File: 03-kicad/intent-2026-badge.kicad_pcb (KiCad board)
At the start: 2 copper layers, 56 x 118 mm, 89 parts, among them J1 TYPE-C-16PIN, J2 HACK HEADER, J3 BATT 3xAAA, J4 PJ-320D, J5 IR, J6 AUDIO, J7 SPK, P1 IR MODULE, P2 AUDIO MODULE, P3 SPK MODULE, Q1 HL3401, Q2 S8050, SW1 BOOTSEL, SW2 A, SW3 B, SW4 C, SW5 MSK12C02, U1 RP2040, U2 W25Q16JVSNIQ, U3 ME6206A33M3G, U4 USBLC6-2SC6, U5 IRM-H638T/TR2, Y1 12MHz

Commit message: Vending-machine theme: themed silkscreen, modules as vended items with shaped outlines
- silk.py: shelf items A1-A4 with price tags over a dispensing coil, keypad bezel + SELECT,
  CREDIT meter with coin values, ITEM PICKUP door around slots B1/B2/B3, coin slot,
  back service-panel texts (SERVICE COMPARTMENT, model plate, NO REFUNDS)
- modules: B1 EYE CANDY candy bar (crimped edges, 1.2 mm chamfers), B2 AUDIO POP soda can
  (R 2.5 corners, bubbles), B3 BEEP CHIPS chips bag (crimped edges, 2 mm chamfers)
- placement.MODULE_CORNERS + pcb_build.module_perimeter/add_module_edges draw the corners
- board, gerbers, renders, DRC/ERC reports regenerated (DRC 0 violations); docs updated

Co-Authored-By: Claude Fable 5.1 <noreply@anthropic.com>
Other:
- outline, holes or cut-outs redrawn
- board text added: "$1"
- board text added: "10¢"
- board text added: "25¢"
- board text added: "38kHz"
- board text added: "50¢"
- board text added: "5¢"
- board text added: "A1 25¢"
- board text added: "A2 50¢"
- board text added: "A3 75¢"
- board text added: "A4 $1"
- board text added: "AUDIO POP · 3.5mm"
- board text added: "AUTHORIZED PERSONNEL ONLY"
- board text added: "B1"
- board text added: "B1 IR"
- board text added: "B1 · IR MODULE"
- board text added: "B2"
- board text added: "B2 AUDIO"
- board text added: "B2 · AUDIO MODULE"
- board text added: "B3"
- board text added: "B3 SPK"
- board text added: "B3 · SPK MODULE"
- board text added: "BEEP CHIPS"
- board text added: "EYE CANDY"
- board text added: "ITEM PICKUP"
- board text added: "MODEL VM-2026 · 3V3 · 2 LAYERS"
- board text added: "NO REFUNDS · DO NOT TILT OR ROCK"
- board text added: "NO USER-SERVICEABLE PARTS INSIDE (JK, SEE J2)"
- board text added: "SELECT"
- board text added: "SERVICE COMPARTMENT"
- board text added: "← PRIZE"
- board text removed: "* PRIZE *"
- board text removed: "AUDIO"
- board text removed: "AUDIO MODULE"
- board text removed: "IR EYE"
- board text removed: "IR MODULE"
- board text removed: "SPK"
- board text removed: "SPK MODULE"

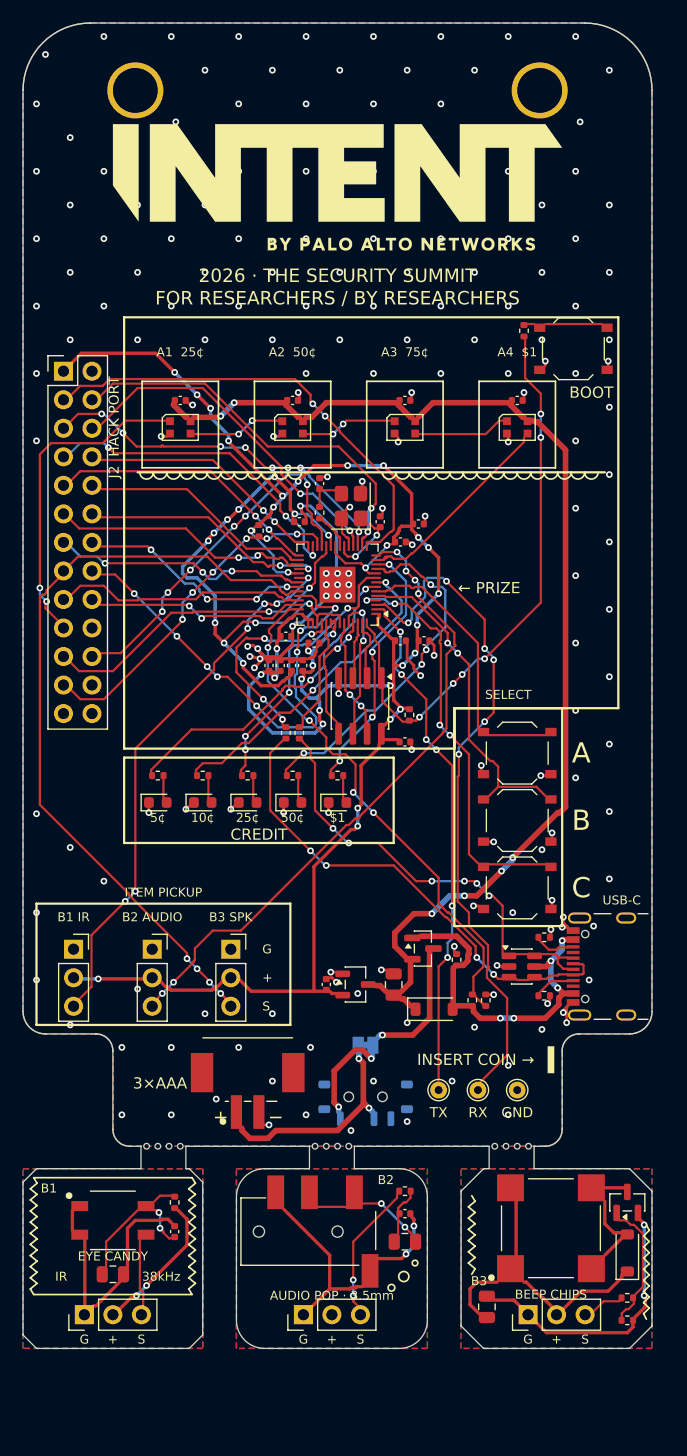
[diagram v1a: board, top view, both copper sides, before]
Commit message: Vending-machine outline: header sign box with lanyard holes, modules as 13x22 mm soda cans
- pcb_build OUTLINE: R6 top replaced by a header sign box x 7-49 x y 0-9 (R2.5 corners, R1 fillets,
  R2 cabinet corners); H1/H2 moved to (12,5.5)/(44,5.5); INTENT-O-MATIC marquee; logo 1 mm lower
- placement: MODULES = cans 13x22 R2.2 at x 5.5/21.5/37.5, tabs 12/28/44, blank 56x124;
  module parts re-placed (header at the can bottom, passives in a row)
- silk: can rims, label band with wave, B1 IR COLA / B2 AUDIO POP / B3 BEEP FIZZ
- router: NY 1270, NET_ONLY mode + router/prune_routes.py for partial re-routes; only module
  nets re-routed (97 tracks, 14 vias), main-board copper unchanged except 8 pruned edge GND vias
- board, gerbers, CPL, renders, reports regenerated: DRC 0 violations, 0 unconnected; docs updated

Co-Authored-By: Claude Fable 5.1 <noreply@anthropic.com>
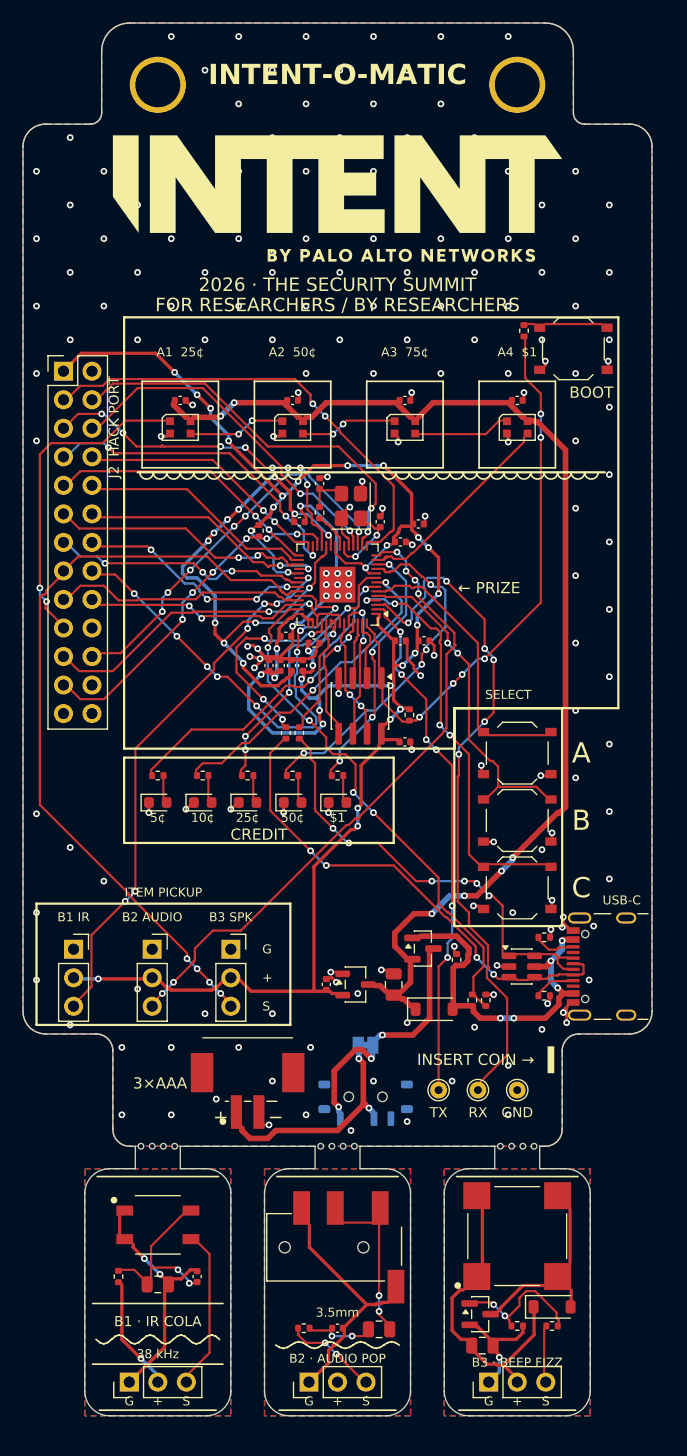
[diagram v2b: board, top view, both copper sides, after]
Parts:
- moved Q2 16.5 mm to (140.7, 164.9), turned to 0 degrees
- moved R17 15.2 mm to (125.0, 166.2)
- moved C21 11.8 mm to (128.0, 166.2)
- moved R21 9.81 mm to (144.0, 166.0)
- moved R19 8.28 mm to (108.5, 161.6)
- moved D7 8.24 mm to (147.1, 164.3), turned to 0 degrees
- moved C22 8.13 mm to (131.7, 166.3)
- moved P1 7.21 mm to (109.5, 171.0)
- moved R20 7.15 mm to (147.1, 166.0)
- moved P3 6.95 mm to (141.5, 171.0)
- moved P2 6.02 mm to (125.5, 171.0)
- moved C23 4.47 mm to (115.5, 161.6)
- moved C24 4.10 mm to (112.0, 162.3)
- moved U5 4.02 mm to (112.0, 157.0)
- moved C25 3.47 mm to (140.9, 167.8), turned to 0 degrees
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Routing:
- net SPM_GND: track 20.9 -> 6.19 mm, vias 2 -> 1
- net IRM_OUT: track 6.02 -> 12.6 mm
- net AUM_PWM: track 11.7 -> 7.23 mm
- net AUM_OUT: track 8.12 -> 11.4 mm
- net SPM_COL: track 7.55 -> 10.8 mm
- net IRM_3V3: track 11.8 -> 9.14 mm, vias 2 -> 1
- net IRM_GND: track 18.8 -> 16.2 mm, vias 0 -> 2
- net IRM_VCC: track 11.2 -> 13.2 mm
- net AUM_GND: track 20.2 -> 18.6 mm, vias 2 -> 0
- net AUM_FILT: track 3.47 -> 4.84 mm, vias 0 -> 2
- net SPM_SIG: track 2.67 -> 3.90 mm
- net SPM_BASE: track 10.3 -> 11.2 mm, vias 0 -> 2
- net GND: vias 194 -> 186
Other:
- board size 56 x 118 mm -> 56 x 124 mm
- board text added: "3.5mm"
- board text added: "38 kHz"
- board text added: "B1 IR MODULE"
- board text added: "B1 · IR COLA"
- board text added: "B2 AUDIO MODULE"
- board text added: "B2 · AUDIO POP"
- board text added: "B3 SPK MODULE"
- board text added: "B3 · BEEP FIZZ"
- board text added: "INTENT-O-MATIC"
- board text added: "plug into J5"
- board text added: "plug into J6"
- board text added: "plug into J7"
- board text added: "snap off,"
- board text removed: "38kHz"
- board text removed: "AUDIO POP · 3.5mm"
- board text removed: "B1"
- board text removed: "B1 · IR MODULE"
- board text removed: "B2"
- board text removed: "B2 · AUDIO MODULE"
- board text removed: "B3"
- board text removed: "B3 · SPK MODULE"
- board text removed: "BEEP CHIPS"
- board text removed: "EYE CANDY"
- board text removed: "IR"
- board text removed: "snap off, plug into J5"
- board text removed: "snap off, plug into J6"
- board text removed: "snap off, plug into J7"

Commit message: Vending-machine art pass: feet, exposed-copper logo/marquee/keys/can rims, product icons, back art
- pcb_build OUTLINE: feet x 0-5.5 / 50.5-56, y 88-94.5 with a 2.5 mm notch to the pedestal (additive)
- art_copper.py (new, called by pcb_finish): INTENT logo, INTENT-O-MATIC, A/B/C, BOOT as F.Cu + F.Mask,
  can rims as mask openings; placement.ART_KEEPOUTS; prune_routes --art drops GND vias there (28)
- silk: product icons around the shelf LEDs, glass glare, coin, pull-tab rings on the can stubs;
  back: three AAA cells, DANGER 3V3 INSIDE sticker, SERVICE LOG
- placement and signal routing unchanged; DRC 0 violations, 0 unconnected; fab outputs, renders, docs
  regenerated; order-spec recommends ENIG for the gold look

Co-Authored-By: Claude Fable 5.1 <noreply@anthropic.com>
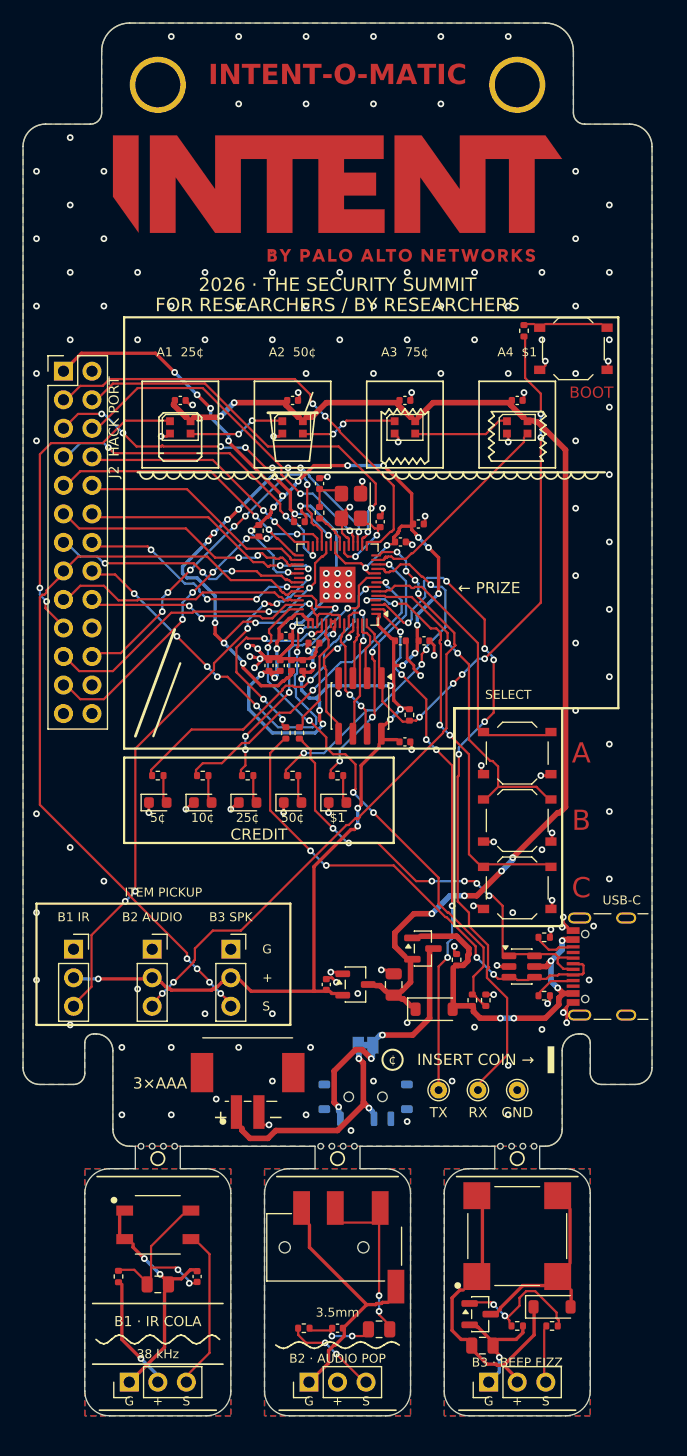
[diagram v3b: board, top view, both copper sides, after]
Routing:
- net GND: vias 186 -> 158
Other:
- outline, holes or cut-outs redrawn
- board text added: "3V3 INSIDE"
- board text added: "3×AAA BATTERY BOX · tape here · switch on box"
- board text added: "AAA"
- board text added: "DANGER"
- board text added: "SERVICE LOG"
- board text added: "¢"
- board text removed: "3×AAA BATTERY BOX"
- board text removed: "tape here · switch on box"

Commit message: Rev 0.6: RP2040 design-guide review, SAO ports, re-layout, hand MCU re-route
Schematic/BOM (design.py, gen_sch.py):
- VREG decoupling per the RP2040 hardware design guide: 1 uF on VREG_VIN (C18)
  and VREG_VOUT (new C26), C10 100 nF on DVDD 50
- Y1 -> ABM8-272-T3 (C20625731), U3 -> AP2112K-3.3 (C51118) with 10 uF out,
  J1 -> HRO TYPE-C-31-M-12 (C165948), VBUS caps C27/C28, RESET button SW6
- RGB data buffer U6 SN74LV1T34 on VSYS (+C29)
- Expansion ports -> SAO 2x3 SMD sockets/headers, I2C0 on GPIO12/13 with
  4.7k pull-ups, GPIO2 on GPIO26-28; C22 now 0603
- ERC 0 errors / 0 warnings, netlist check 0 problems

PCB (placement.py, silk.py, art_copper.py, route2.py):
- RP2040 core re-placed after the guide (VREG caps and 27R next to the pins,
  QSPI_SS resistors at the flash), new parts placed, silk updated
- Router treats the exposed-copper art as a hard keepout
- Board as committed includes Benny's hand re-route of the MCU area in KiCad;
  build/routes.json and 04-fab are from the scripted route (BUILD-NOTES 16/17)

Also: review report (01-spec), BOM deltas EN/HE, GPIO map, Windows build
scripts (scripts/win), rev 0.5 fab outputs archived.

Co-Authored-By: Claude Opus 5.5 (1M context) <noreply@anthropic.com>
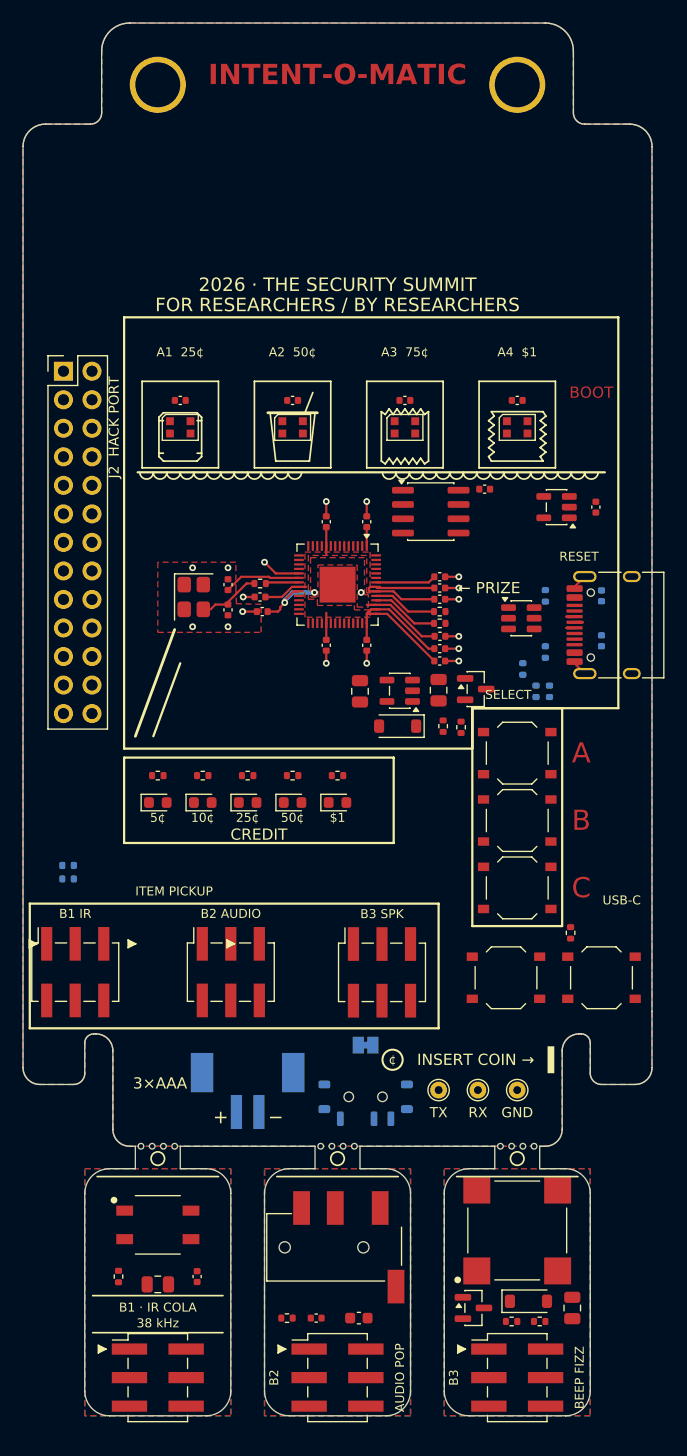
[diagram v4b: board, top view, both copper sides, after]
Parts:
- added C26: 1uF, Capacitor_SMD:C_0402_1005Metric, F.Cu at (137.1, 104.6)
- added C27: 1uF, Capacitor_SMD:C_0402_1005Metric, B.Cu at (151.5, 105.0)
- added C28: 100nF, Capacitor_SMD:C_0402_1005Metric, B.Cu at (151.5, 101.0)
- added C29: 100nF, Capacitor_SMD:C_0402_1005Metric, F.Cu at (151.0, 93.1)
- added R22: 4.7k, Resistor_SMD:R_0402_1005Metric, B.Cu at (104.0, 125.0)
- added R23: 4.7k, Resistor_SMD:R_0402_1005Metric, B.Cu at (104.0, 126.2)
- added SW6: RESET, Button_Switch_SMD:SW_Push_1P1T_XKB_TS-1187A, F.Cu at (151.5, 135.0)
- added U6: SN74LV1T34DBVR, Package_TO_SOT_SMD:SOT-23-5, F.Cu at (147.5, 93.1)
- C10: value 1uF -> 100nF
- C18: value 100nF -> 1uF
- C20: value 1uF -> 10uF; footprint Capacitor_SMD:C_0402_1005Metric -> Capacitor_SMD:C_0805_2012Metric
- C22: footprint Capacitor_SMD:C_0805_2012Metric -> Capacitor_SMD:C_0603_1608Metric
- J1: value TYPE-C-16PIN -> TYPE-C-31-M-12; footprint intent:USB_C_TYPE-C16PIN_C393939 -> Connector_USB:USB_C_Receptacle_HRO_TYPE-C-31-M-12
- J3, R1, R10, R15, R16, R2: moved to B.Cu
- J5: value IR -> SAO1 IR; footprint Connector_PinSocket_2.54mm:PinSocket_1x03_P2.54mm_Vertical -> Connector_PinSocket_2.54mm:PinSocket_2x03_P2.54mm_Vertical_SMD
- J6: value AUDIO -> SAO2 AUDIO; footprint Connector_PinSocket_2.54mm:PinSocket_1x03_P2.54mm_Vertical -> Connector_PinSocket_2.54mm:PinSocket_2x03_P2.54mm_Vertical_SMD
- J7: value SPK -> SAO3 SPK; footprint Connector_PinSocket_2.54mm:PinSocket_1x03_P2.54mm_Vertical -> Connector_PinSocket_2.54mm:PinSocket_2x03_P2.54mm_Vertical_SMD
- P1, P2, P3: footprint Connector_PinHeader_2.54mm:PinHeader_1x03_P2.54mm_Vertical -> Connector_PinHeader_2.54mm:PinHeader_2x03_P2.54mm_Vertical_SMD
- U3: value ME6206A33M3G -> AP2112K-3.3TRG1; footprint Package_TO_SOT_SMD:SOT-23-3 -> Package_TO_SOT_SMD:SOT-23-5
- Y1: value 12MHz -> 12MHz ABM8-272-T3
- moved SW1 56.3 mm to (143.0, 135.0)
- moved R4 45.3 mm to (148.8, 131.0)
- moved R14 35.7 mm to (139.0, 112.7)
- moved U4 31.0 mm to (144.4, 103.0)
- moved R1 30.6 mm to (146.5, 106.0), turned to -90 degrees
- moved J1 30.5 mm to (153.2, 103.6)
- moved R2 30.4 mm to (146.5, 101.0), turned to 90 degrees
- moved R15 28.3 mm to (146.9, 109.5)
- moved R16 27.9 mm to (145.7, 109.5)
- moved R10 26.6 mm to (144.5, 107.5)
- moved C9 26.5 mm to (137.0, 109.4), turned to -90 degrees
- moved U3 26.4 mm to (133.5, 109.5), turned to 180 degrees
- moved C20 26.3 mm to (130.0, 109.5), turned to -90 degrees
- moved D6 25.4 mm to (133.3, 112.6), turned to 180 degrees
- moved C6 23.6 mm to (141.1, 91.5)
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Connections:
- J2 pad 16: GPIO26 -> SAO1_GPIO2
- J2 pad 17: GPIO27 -> SAO2_GPIO2
- J2 pad 18: GPIO28 -> SAO3_GPIO2
- J2 pad 3: GPIO12 -> SAO_SDA
- J2 pad 4: GPIO13 -> SAO_SCL
- J5 pad 1: GND -> +3V3
- J5 pad 2: +3V3 -> GND
- J5 pad 3: IR_OUT -> SAO_SDA
- J6 pad 1: GND -> +3V3
- J6 pad 2: +3V3 -> GND
- J6 pad 3: AUDIO_PWM -> SAO_SDA
- J7 pad 1: GND -> +3V3
- J7 pad 2: +3V3 -> GND
- J7 pad 3: SPK_PWM -> SAO_SDA
- P1 pad 1: IRM_GND -> IRM_3V3
- P1 pad 2: IRM_3V3 -> IRM_GND
- P1 pad 3: IRM_OUT -> unconnected-(P1-Pin_3-Pad3)
- P2 pad 1: AUM_GND -> unconnected-(P2-Pin_1-Pad1)
- P2 pad 2: unconnected-(P2-Pin_2-Pad2) -> AUM_GND
- P2 pad 3: AUM_PWM -> unconnected-(P2-Pin_3-Pad3)
- P3 pad 1: SPM_GND -> SPM_3V3
- P3 pad 2: SPM_3V3 -> SPM_GND
- P3 pad 3: SPM_SIG -> unconnected-(P3-Pin_3-Pad3)
- U1 pad 13: RGB_DIN -> RGB_CTRL
- U1 pad 15: GPIO12 -> SAO_SDA
- U1 pad 16: GPIO13 -> SAO_SCL
- U1 pad 38: GPIO26 -> SAO1_GPIO2
- U1 pad 39: GPIO27 -> SAO2_GPIO2
- U1 pad 40: GPIO28 -> SAO3_GPIO2
- U3 pad 1: GND -> VSYS
- U3 pad 2: +3V3 -> GND
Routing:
- net +3V3: track 171.9 -> 40.5 mm, vias 34 -> 0
- net VSYS: track 96.4 -> 0.00 mm, vias 6 -> 0
- net SPK_PWM: track 67.0 -> 0.00 mm, vias 4 -> 0
- net UART0_RX: track 60.5 -> 0.00 mm, vias 6 -> 0
- net AUDIO_PWM: track 56.4 -> 0.00 mm, vias 6 -> 0
- net QSPI_SS: track 47.8 -> 0.00 mm, vias 6 -> 0
- net IR_OUT: track 47.5 -> 0.00 mm, vias 6 -> 0
- net VBUS_SENSE: track 45.9 -> 0.00 mm, vias 4 -> 0
- net GND: track 66.7 -> 20.8 mm, vias 158 -> 17
- net UART0_TX: track 45.8 -> 0.00 mm, vias 6 -> 0
- net GPIO26: track 41.7 -> 0.00 mm, vias 8 -> 0
- net GPIO12: track 40.3 -> 0.00 mm, vias 2 -> 0
- net USB_DM_CONN: track 39.2 -> 0.72 mm, vias 4 -> 0
- net BTN_C: track 35.5 -> 0.00 mm, vias 4 -> 0
- net USB_DP_CONN: track 36.1 -> 1.45 mm, vias 6 -> 0
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- added copper zone on F.Cu, net +1V1
- added copper zone on F.Cu, net +3V3
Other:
- board text added: "AUDIO POP"
- board text added: "B2"
- board text added: "B3"
- board text added: "BEEP FIZZ"
- board text added: "Benny Meisels"
- board text added: "INTENT 2026 badge · rev 0.6 · 2026-10"
- board text added: "RESET"
- board text removed: "3.5mm"
- board text removed: "B2 · AUDIO POP"
- board text removed: "B3 · BEEP FIZZ"
- board text removed: "Benny Mizels"
- board text removed: "G"
- board text removed: "INTENT 2026 badge · rev 0.5 · 2026-10"
- board text removed: "S"
